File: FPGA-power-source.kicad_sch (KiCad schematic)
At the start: 34 parts, among them U1 TPS54325PWPR, U2 TPS54294PWP

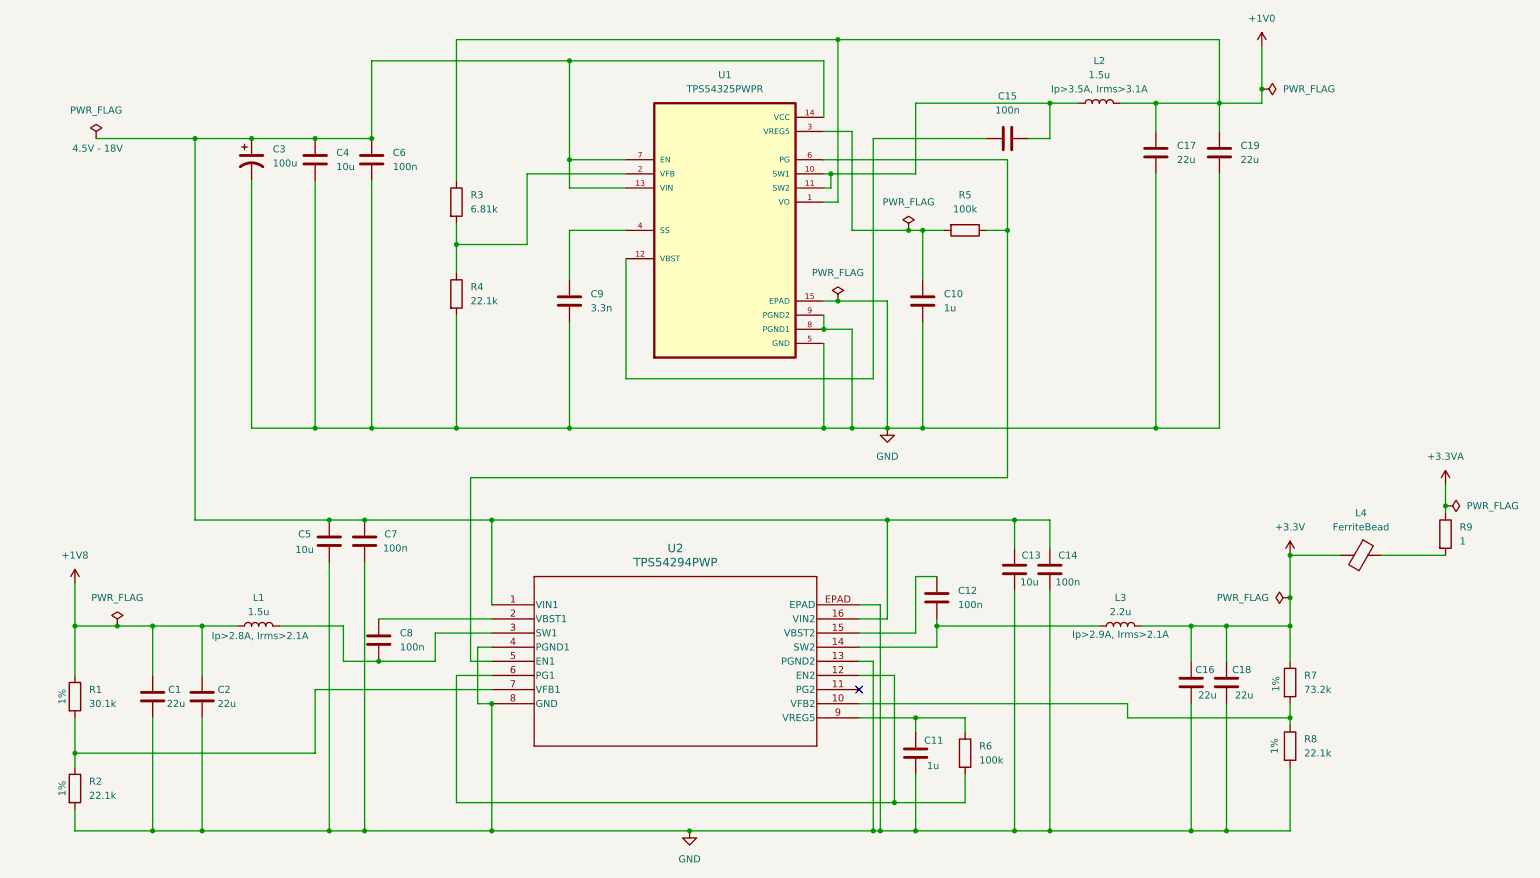
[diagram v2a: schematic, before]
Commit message: schematic for stm32u545
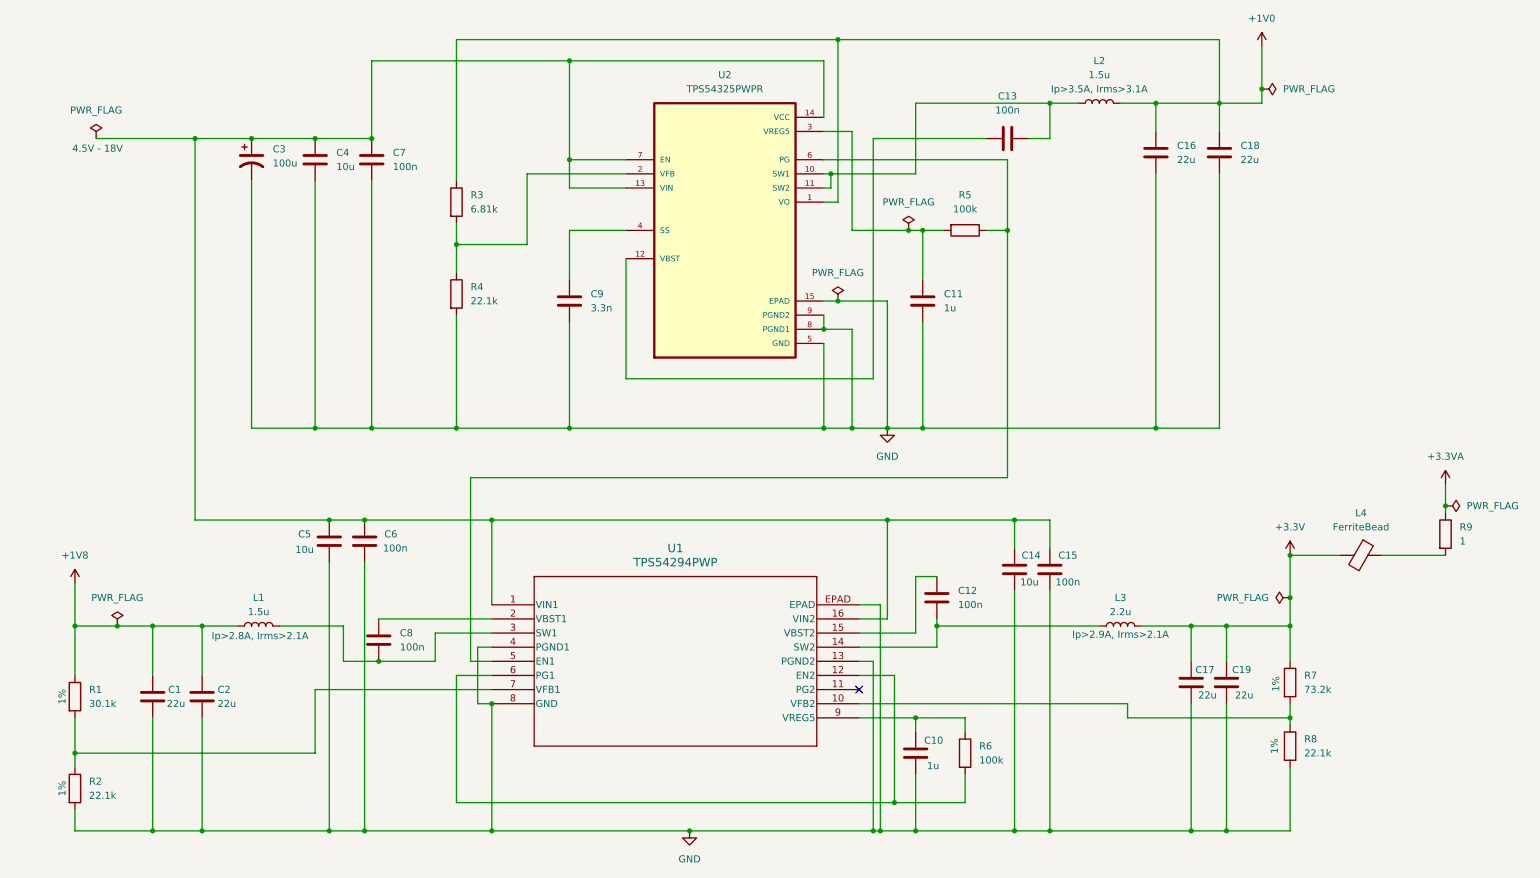
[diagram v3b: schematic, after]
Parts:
- renumbered C11 to C10, C10 to C11, C15 to C13, C13 to C14, C14 to C15, C17 to C16, C16 to C17, C19 to C18, C18 to C19, C7 to C6, C6 to C7, U2 to U1, U1 to U2
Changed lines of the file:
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@@
 		(dnp no)
 		(fields_autoplaced yes)
-		(property "Reference" "C10"
+		(property "Reference" "C11"
 			(at 180.34 63.4999 0)
 			(effects
@@
 			(project ""
 				(path "/071102f3-276b-4b6b-8738-8c534a30b197/f7dbf63d-f891-4c8e-a7a2-66a57df960da"
-					(reference "C10")
+					(reference "C11")
 					(unit 1)
 				)
@@
 		(dnp no)
 		(fields_autoplaced yes)
-		(property "Reference" "#PWR04"
+		(property "Reference" "#PWR02"
 			(at 134.62 166.37 0)
 			(effects
@@
 			(project ""
 				(path "/071102f3-276b-4b6b-8738-8c534a30b197/f7dbf63d-f891-4c8e-a7a2-66a57df960da"
-					(reference "#PWR04")
+					(reference "#PWR02")
 					(unit 1)
 				)
@@
 		(on_board yes)
 		(dnp no)
-		(property "Reference" "C7"
+		(property "Reference" "C6"
 			(at 79.756 106.68 0)
 			(effects
@@
 			(project ""
 				(path "/071102f3-276b-4b6b-8738-8c534a30b197/f7dbf63d-f891-4c8e-a7a2-66a57df960da"
-					(reference "C7")
+					(reference "C6")
 					(unit 1)
 				)
@@
 		(dnp no)
 		(fields_autoplaced yes)
-		(property "Reference" "C15"
+		(property "Reference" "C13"
 			(at 191.77 27.94 90)
 			(effects
@@
 			(project ""
 				(path "/071102f3-276b-4b6b-8738-8c534a30b197/f7dbf63d-f891-4c8e-a7a2-66a57df960da"
-					(reference "C15")
+					(reference "C13")
 					(unit 1)
 				)
@@
 		(dnp no)
 		(fields_autoplaced yes)
-		(property "Reference" "U2"
+		(property "Reference" "U1"
 			(at 132.08 109.22 0)
 			(effects
@@
 			(project ""
 				(path "/071102f3-276b-4b6b-8738-8c534a30b197/f7dbf63d-f891-4c8e-a7a2-66a57df960da"
-					(reference "U2")
+					(reference "U1")
 					(unit 1)
 				)
@@
 		(dnp no)
 		(fields_autoplaced yes)
-		(property "Reference" "#FLG05"
+		(property "Reference" "#FLG02"
 			(at 31.75 121.285 0)
 			(effects
@@
 			(project ""
 				(path "/071102f3-276b-4b6b-8738-8c534a30b197/f7dbf63d-f891-4c8e-a7a2-66a57df960da"
-					(reference "#FLG05")
+					(reference "#FLG02")
 					(unit 1)
 				)
@@
 		(dnp no)
 		(fields_autoplaced yes)
-		(property "Reference" "#FLG06"
+		(property "Reference" "#FLG04"
 			(at 173.99 50.165 0)
 			(effects
@@
 			(project ""
 				(path "/071102f3-276b-4b6b-8738-8c534a30b197/f7dbf63d-f891-4c8e-a7a2-66a57df960da"
-					(reference "#FLG06")
+					(reference "#FLG04")
 					(unit 1)
 				)
@@
 		(dnp no)
 		(fields_autoplaced yes)
-		(property "Reference" "#FLG04"
+		(property "Reference" "#FLG06"
 			(at 240.665 118.11 0)
 			(effects
@@
 			(project ""
 				(path "/071102f3-276b-4b6b-8738-8c534a30b197/f7dbf63d-f891-4c8e-a7a2-66a57df960da"
-					(reference "#FLG04")
+					(reference "#FLG06")
 					(unit 1)
 				)
@@
 		(dnp no)
 		(fields_autoplaced yes)
-		(property "Reference" "#PWR02"
+		(property "Reference" "#PWR03"
 			(at 170.18 93.98 0)
 			(effects
@@
 			(project ""
 				(path "/071102f3-276b-4b6b-8738-8c534a30b197/f7dbf63d-f891-4c8e-a7a2-66a57df960da"
-					(reference "#PWR02")
+					(reference "#PWR03")
 					(unit 1)
 				)
@@
 		(on_board yes)
 		(dnp no)
-		(property "Reference" "C18"
+		(property "Reference" "C19"
 			(at 232.156 131.064 0)
 			(effects
@@
 			(project ""
 				(path "/071102f3-276b-4b6b-8738-8c534a30b197/f7dbf63d-f891-4c8e-a7a2-66a57df960da"
-					(reference "C18")
+					(reference "C19")
 					(unit 1)
 				)
@@
 		(dnp no)
 		(fields_autoplaced yes)
-		(property "Reference" "C17"
+		(property "Reference" "C16"
 			(at 222.25 36.8299 0)
 			(effects
@@
 			(project ""
 				(path "/071102f3-276b-4b6b-8738-8c534a30b197/f7dbf63d-f891-4c8e-a7a2-66a57df960da"
-					(reference "C17")
+					(reference "C16")
 					(unit 1)
 				)
@@
 		(dnp no)
 		(fields_autoplaced yes)
-		(property "Reference" "#PWR03"
+		(property "Reference" "#PWR01"
 			(at 24.13 119.38 0)
 			(effects
@@
 			(project ""
 				(path "/071102f3-276b-4b6b-8738-8c534a30b197/f7dbf63d-f891-4c8e-a7a2-66a57df960da"
-					(reference "#PWR03")
+					(reference "#PWR01")
 					(unit 1)
 				)
@@
 		(dnp no)
 		(fields_autoplaced yes)
-		(property "Reference" "#FLG02"
+		(property "Reference" "#FLG07"
 			(at 272.415 101.6 0)
 			(effects
@@
 			(project ""
 				(path "/071102f3-276b-4b6b-8738-8c534a30b197/f7dbf63d-f891-4c8e-a7a2-66a57df960da"
-					(reference "#FLG02")
+					(reference "#FLG07")
 					(unit 1)
 				)
@@
 		(on_board yes)
 		(dnp no)
-		(property "Reference" "C11"
+		(property "Reference" "C10"
 			(at 176.784 143.764 0)
 			(effects
@@
 			(project ""
 				(path "/071102f3-276b-4b6b-8738-8c534a30b197/f7dbf63d-f891-4c8e-a7a2-66a57df960da"
-					(reference "C11")
+					(reference "C10")
 					(unit 1)
 				)
@@
 		(dnp no)
 		(fields_autoplaced yes)
-		(property "Reference" "C6"
+		(property "Reference" "C7"
 			(at 81.28 38.0999 0)
 			(effects
@@
 			(project ""
 				(path "/071102f3-276b-4b6b-8738-8c534a30b197/f7dbf63d-f891-4c8e-a7a2-66a57df960da"
-					(reference "C6")
+					(reference "C7")
 					(unit 1)
 				)
@@
 		(dnp no)
 		(fields_autoplaced yes)
-		(property "Reference" "#FLG07"
+		(property "Reference" "#FLG03"
 			(at 161.29 62.865 0)
 			(effects
@@
 			(project ""
 				(path "/071102f3-276b-4b6b-8738-8c534a30b197/f7dbf63d-f891-4c8e-a7a2-66a57df960da"
-					(reference "#FLG07")
+					(reference "#FLG03")
 					(unit 1)
 				)
@@
 		(on_board yes)
 		(dnp no)
-		(property "Reference" "C13"
+		(property "Reference" "C14"
 			(at 194.31 110.49 0)
 			(effects
@@
 			(project ""
 				(path "/071102f3-276b-4b6b-8738-8c534a30b197/f7dbf63d-f891-4c8e-a7a2-66a57df960da"
-					(reference "C13")
+					(reference "C14")
 					(unit 1)
 				)
@@
 		(dnp no)
 		(fields_autoplaced yes)
-		(property "Reference" "#PWR01"
+		(property "Reference" "#PWR04"
 			(at 237.49 22.86 0)
 			(effects
@@
 			(project ""
 				(path "/071102f3-276b-4b6b-8738-8c534a30b197/f7dbf63d-f891-4c8e-a7a2-66a57df960da"
-					(reference "#PWR01")
+					(reference "#PWR04")
 					(unit 1)
 				)
@@
 		(on_board yes)
 		(dnp no)
-		(property "Reference" "C14"
+		(property "Reference" "C15"
 			(at 200.914 110.49 0)
 			(effects
@@
 			(project ""
 				(path "/071102f3-276b-4b6b-8738-8c534a30b197/f7dbf63d-f891-4c8e-a7a2-66a57df960da"
-					(reference "C14")
+					(reference "C15")
 					(unit 1)
 				)
@@
 		(dnp no)
 		(fields_autoplaced yes)
-		(property "Reference" "#FLG03"
+		(property "Reference" "#FLG05"
 			(at 239.395 26.67 0)
 			(effects
@@
 			(project ""
 				(path "/071102f3-276b-4b6b-8738-8c534a30b197/f7dbf63d-f891-4c8e-a7a2-66a57df960da"
-					(reference "#FLG03")
+					(reference "#FLG05")
 					(unit 1)
 				)
@@
 		(on_board yes)
 		(dnp no)
-		(property "Reference" "C16"
+		(property "Reference" "C17"
 			(at 225.552 131.064 0)
 			(effects
@@
 			(project ""
 				(path "/071102f3-276b-4b6b-8738-8c534a30b197/f7dbf63d-f891-4c8e-a7a2-66a57df960da"
-					(reference "C16")
+					(reference "C17")
 					(unit 1)
 				)
@@
 		(dnp no)
 		(fields_autoplaced yes)
-		(property "Reference" "C19"
+		(property "Reference" "C18"
 			(at 233.68 36.8299 0)
 			(effects
@@
 			(project ""
 				(path "/071102f3-276b-4b6b-8738-8c534a30b197/f7dbf63d-f891-4c8e-a7a2-66a57df960da"
-					(reference "C19")
+					(reference "C18")
 					(unit 1)
 				)
@@
 		(dnp no)
 		(fields_autoplaced yes)
-		(property "Reference" "U1"
+		(property "Reference" "U2"
 			(at 140.97 24.13 0)
 			(effects
@@
 			(project ""
 				(path "/071102f3-276b-4b6b-8738-8c534a30b197/f7dbf63d-f891-4c8e-a7a2-66a57df960da"
-					(reference "U1")
-					(unit 1)
-				)
+					(reference "U2")
+					(unit 1)
+				)

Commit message: Fixed schematic comments
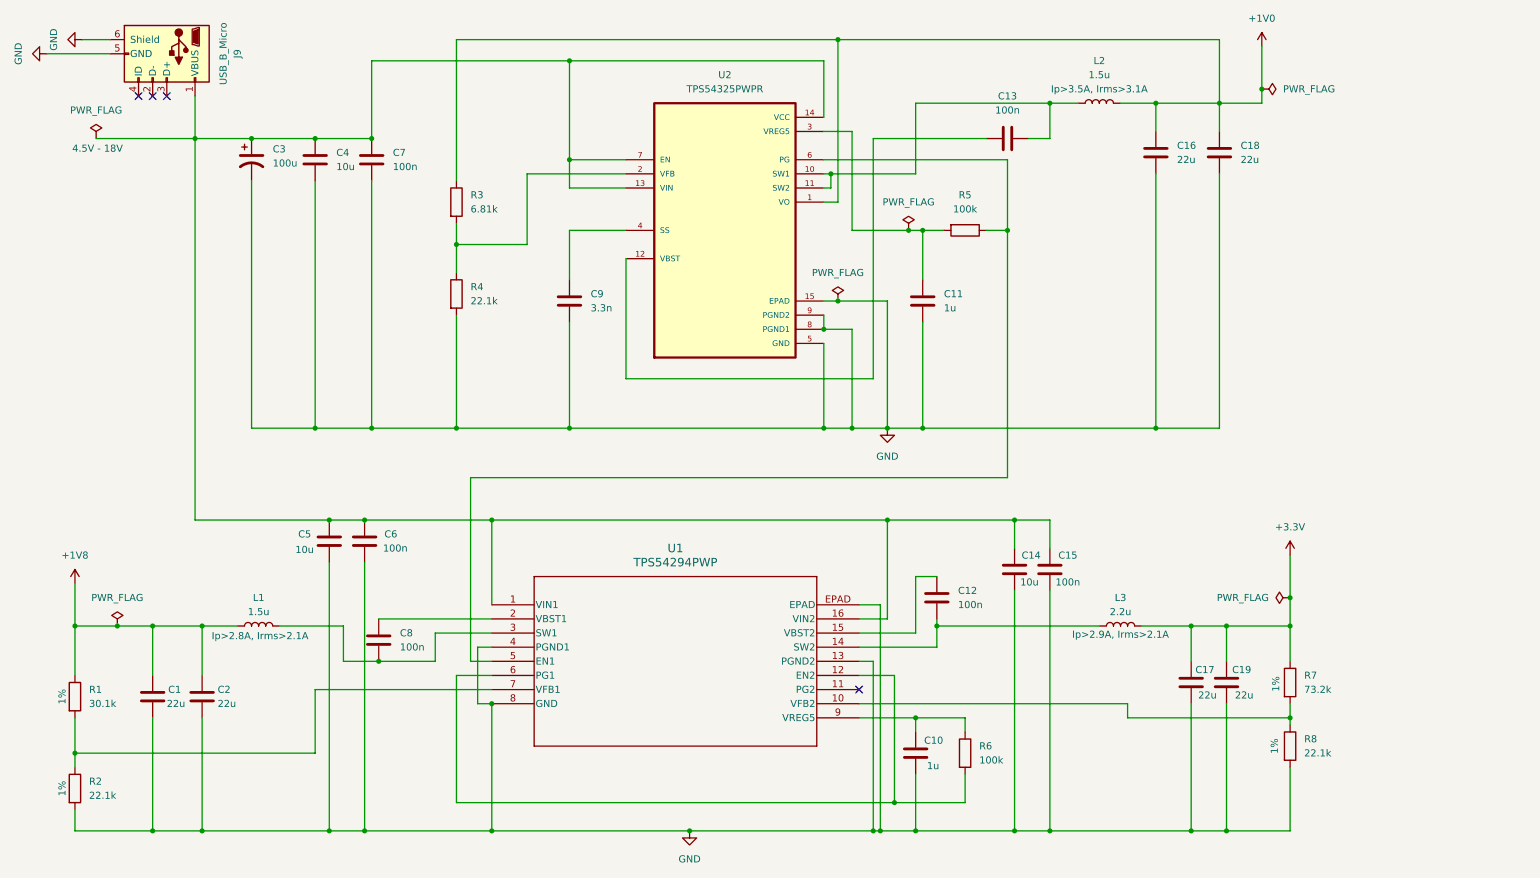
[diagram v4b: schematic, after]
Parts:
- removed L4: FerriteBead, symbol Device:FerriteBead
- removed R9: 1, Resistor_SMD:R_0805_2012Metric, symbol Device:R
- added J9: USB_B_Micro, micro_usbb:CONN_10118192-0002LF_AMP, symbol Connector:USB_B_Micro
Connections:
- net GND: now also J9.5 (GND), J9.6 (Shield)
- net at C14.1, C15.1, C3.1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: now also J9.1 (VBUS)
- no-connect marks 1 -> 4
